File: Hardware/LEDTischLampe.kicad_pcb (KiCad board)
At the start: 2 copper layers, 160 x 160 mm, 135 parts, among them J1 Conn_01x02_Socket, J2 USB_C_Receptacle_USB2.0_14P, J3 Conn_02x03_Counter_Clockwise, Q1 P-CHANNEL-MOSFET, SW1 Reset, SW2 User, U1 ESP32-C3-WROOM-02, U2 SY7200AABC, U3 SY7200AABC, U4 SY7200AABC, U5 SY7200AABC, U6 SY7200AABC, U7 RY8310

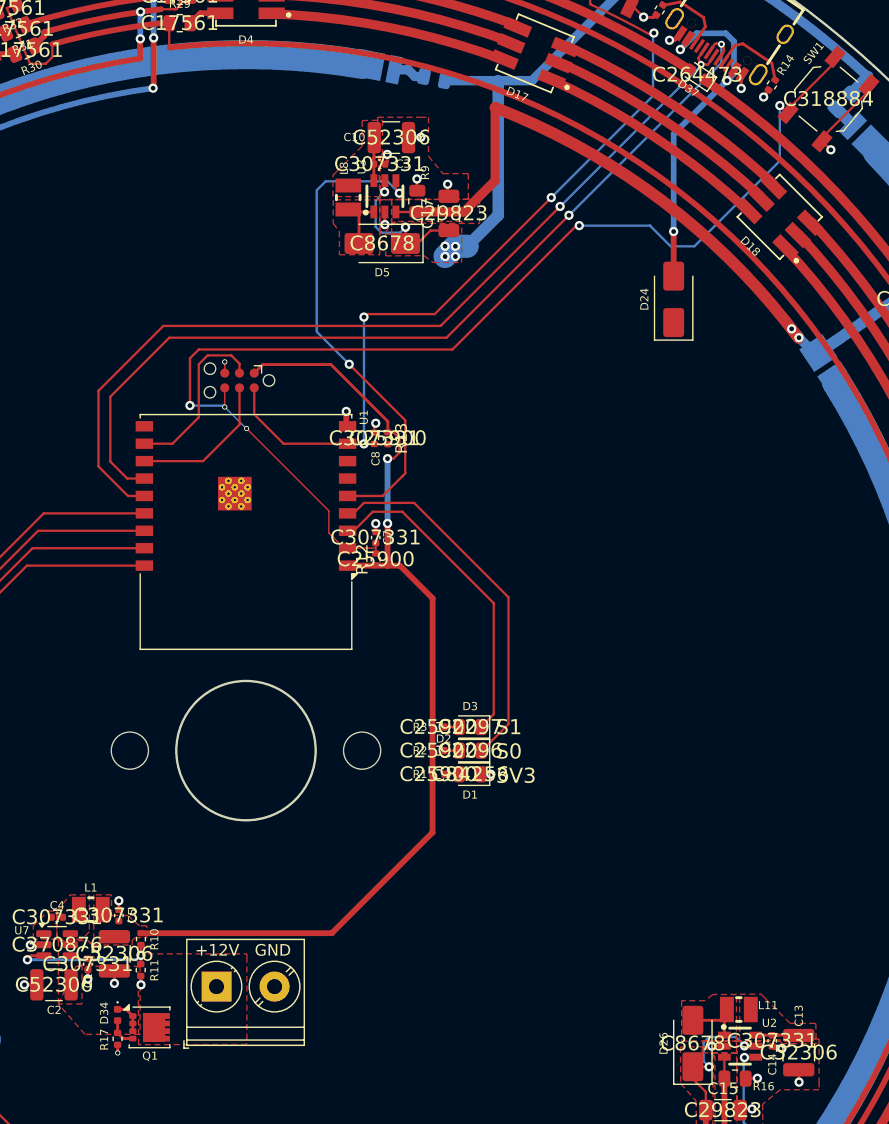
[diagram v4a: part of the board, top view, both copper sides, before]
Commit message: assign remaining LCSC numbers and change R_sense of LED drivers
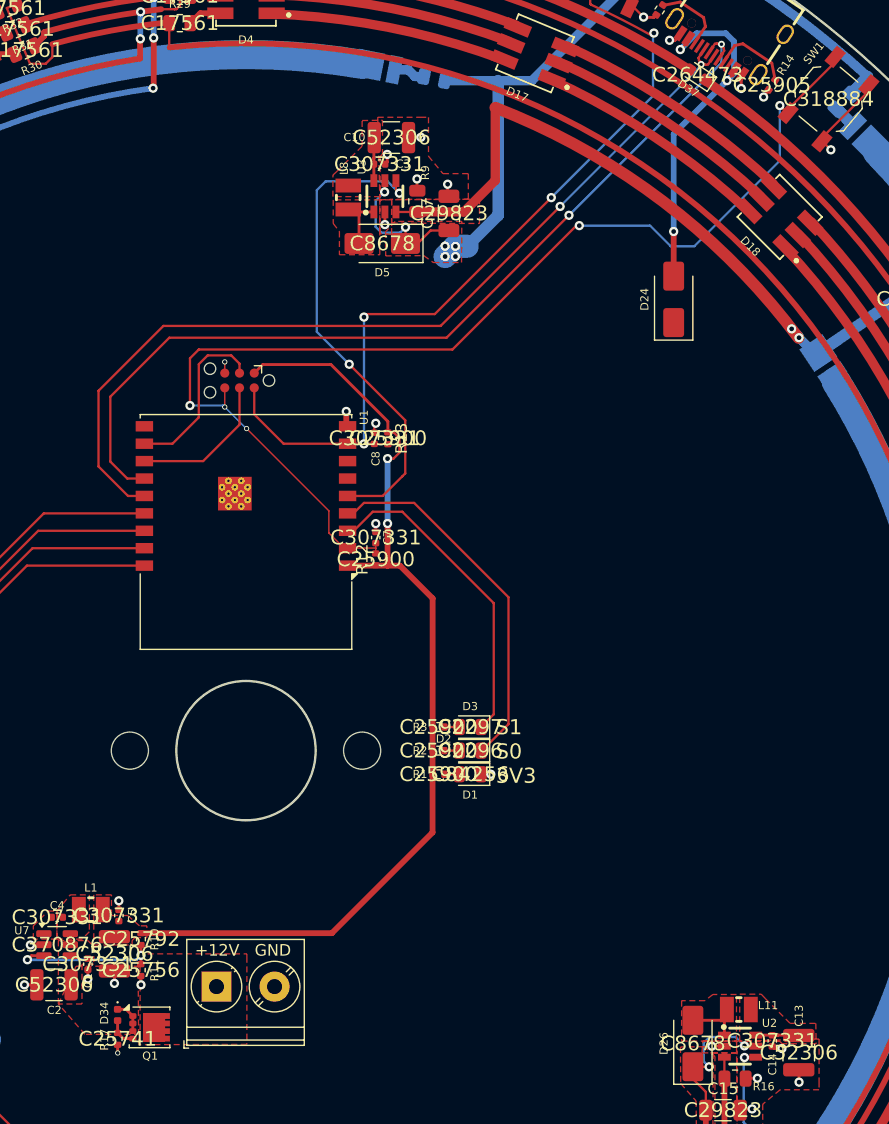
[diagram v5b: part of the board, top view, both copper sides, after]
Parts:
- R16, R26, R27, R8: value 2 -> 3.3
- R9: value 2 -> 0.5
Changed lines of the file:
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@@
 		(sheetname "Root")
 		(sheetfile "LEDTischLampe.kicad_sch")
-		(attr exclude_from_pos_files)
+		(attr exclude_from_pos_files exclude_from_bom)
 		(fp_line
 			(start -1.27 1.27)
@@
 			)
 		)
-		(property "Value" "2"
+		(property "Value" "3.3"
 			(at 0 1.65 0)
 			(layer "F.Fab")
@@
 			)
 		)
-		(property "Description" "Resistor"
+		(property "Description" "Resistor, small symbol"
 			(at 0 0 0)
 			(unlocked yes)
@@
 		)
 		(property ki_fp_filters "R_*")
-		(sheetname "LedTreiber2")
-		(sheetfile "CCLedTreiber.kicad_sch")
+		(sheetname "LedsOben")
+		(sheetfile "LedsOben.kicad_sch")
 		(attr smd)
 		(fp_line
@@
 			)
 		)
+		(property "LCSC" "C25792"
+			(at 0 0 0)
+			(layer "F.SilkS")
+			(effects
+				(font
+					(size 1.27 1.27)
+					(thickness 0.15)
+				)
+			)
+		)
 		(property ki_fp_filters "R_*")
 		(sheetname "Root")
@@
 			)
 		)
+		(property "LCSC" "C25756"
+			(at 0 0 0)
+			(layer "F.SilkS")
+			(effects
+				(font
+					(size 1.27 1.27)
+					(thickness 0.15)
+				)
+			)
+		)
 		(property ki_fp_filters "R_*")
 		(sheetname "Root")
@@
 			)
 		)
-		(property "Value" "2"
+		(property "Value" "0.5"
 			(at 0 1.65 90)
 			(layer "F.Fab")
@@
 			)
 		)
-		(property "Description" "Resistor"
+		(property "Description" "Resistor, small symbol"
 			(at 0 0 90)
 			(unlocked yes)
@@
 		)
 		(property ki_fp_filters "R_*")
-		(sheetname "LedTreiber4")
-		(sheetfile "CCLedTreiber.kicad_sch")
+		(sheetname "LedsUnten")
+		(sheetfile "LedsUnten.kicad_sch")
 		(attr smd)
 		(fp_line
@@
 			)
 		)
+		(property "LCSC" "C25741"
+			(at 0 0 0)
+			(layer "F.SilkS")
+			(effects
+				(font
+					(size 1.27 1.27)
+					(thickness 0.15)
+				)
+			)
+		)
 		(property ki_fp_filters "R_*")
 		(sheetname "Root")
@@
 			)
 		)
+		(property "LCSC" "C25905"
+			(at 0 0 0)
+			(layer "F.SilkS")
+			(effects
+				(font
+					(size 1.27 1.27)
+					(thickness 0.15)
+				)
+			)
+		)
 		(property ki_fp_filters "R_*")
 		(sheetname "Root")
@@
 			)
 		)
-		(property "Value" "2"
+		(property "Value" "3.3"
 			(at 0 1.65 0)
 			(layer "F.Fab")
@@
 			)
 		)
-		(property "Description" "Resistor"
+		(property "Description" "Resistor, small symbol"
 			(at 0 0 0)
 			(unlocked yes)
@@
 		)
 		(property ki_fp_filters "R_*")
-		(sheetname "LedTreiber5")
-		(sheetfile "CCLedTreiber.kicad_sch")
+		(sheetname "LedsOben")
+		(sheetfile "LedsOben.kicad_sch")
 		(attr smd)
 		(fp_line
@@
 			)
 		)
-		(property "Value" "2"
+		(property "Value" "3.3"
 			(at 0 1.65 0)
 			(layer "F.Fab")
@@
 			)
 		)
-		(property "Description" "Resistor"
+		(property "Description" "Resistor, small symbol"
 			(at 0 0 0)
 			(unlocked yes)
@@
 		)
 		(property ki_fp_filters "R_*")
-		(sheetname "LedTreiber3")
-		(sheetfile "CCLedTreiber.kicad_sch")
+		(sheetname "LedsOben")
+		(sheetfile "LedsOben.kicad_sch")
 		(attr smd)
 		(fp_line
@@
 			)
 		)
-		(property "Value" "2"
+		(property "Value" "3.3"
 			(at 0 1.65 0)
 			(layer "F.Fab")
@@
 			)
 		)
-		(property "Description" "Resistor"
+		(property "Description" "Resistor, small symbol"
 			(at 0 0 0)
 			(unlocked yes)
@@
 		)
 		(property ki_fp_filters "R_*")
-		(sheetname "LedTreiber1")
-		(sheetfile "CCLedTreiber.kicad_sch")
+		(sheetname "LedsOben")
+		(sheetfile "LedsOben.kicad_sch")
 		(attr smd)
 		(fp_line

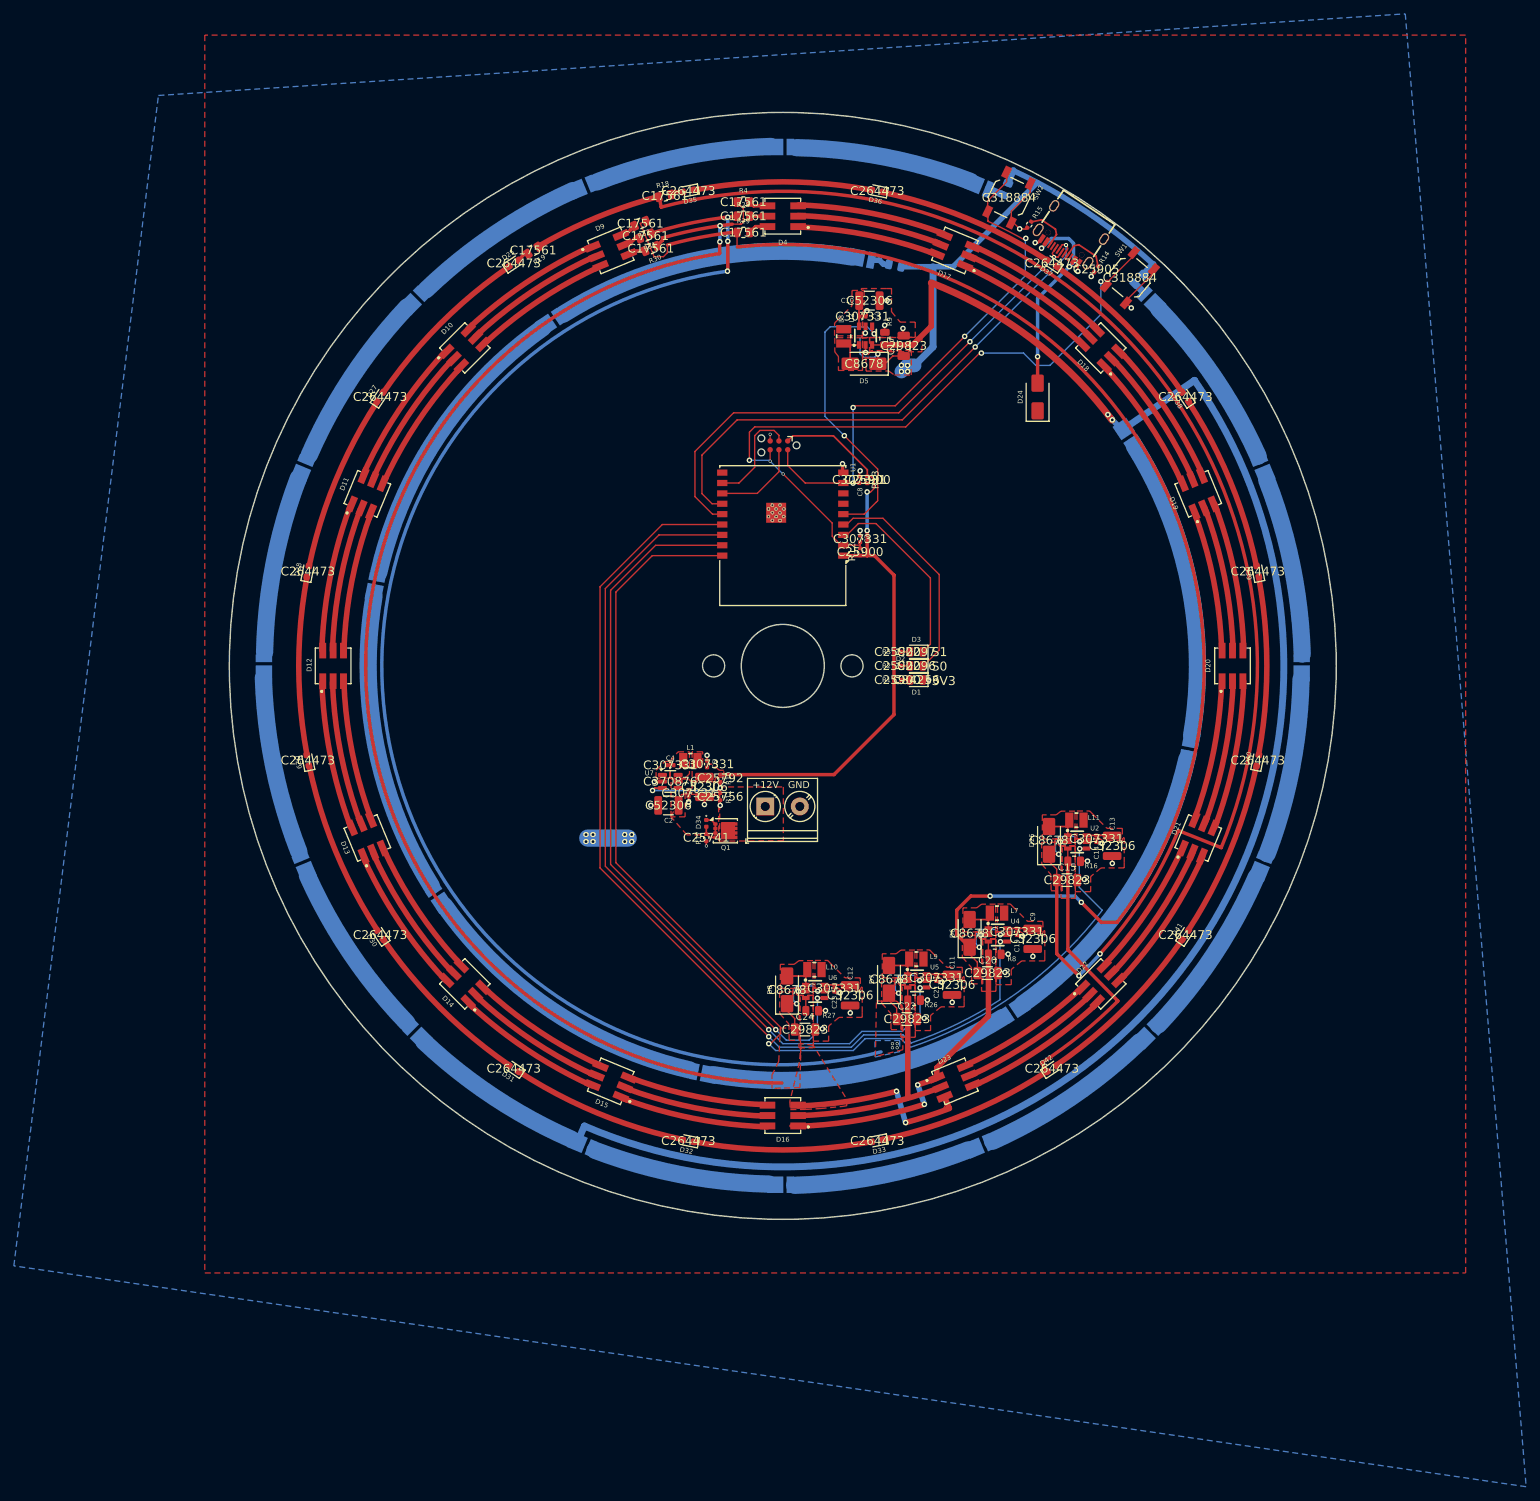
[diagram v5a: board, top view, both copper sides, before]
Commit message: remove LCSC numbers from silkscreen (bug in jlcpcb-tools)
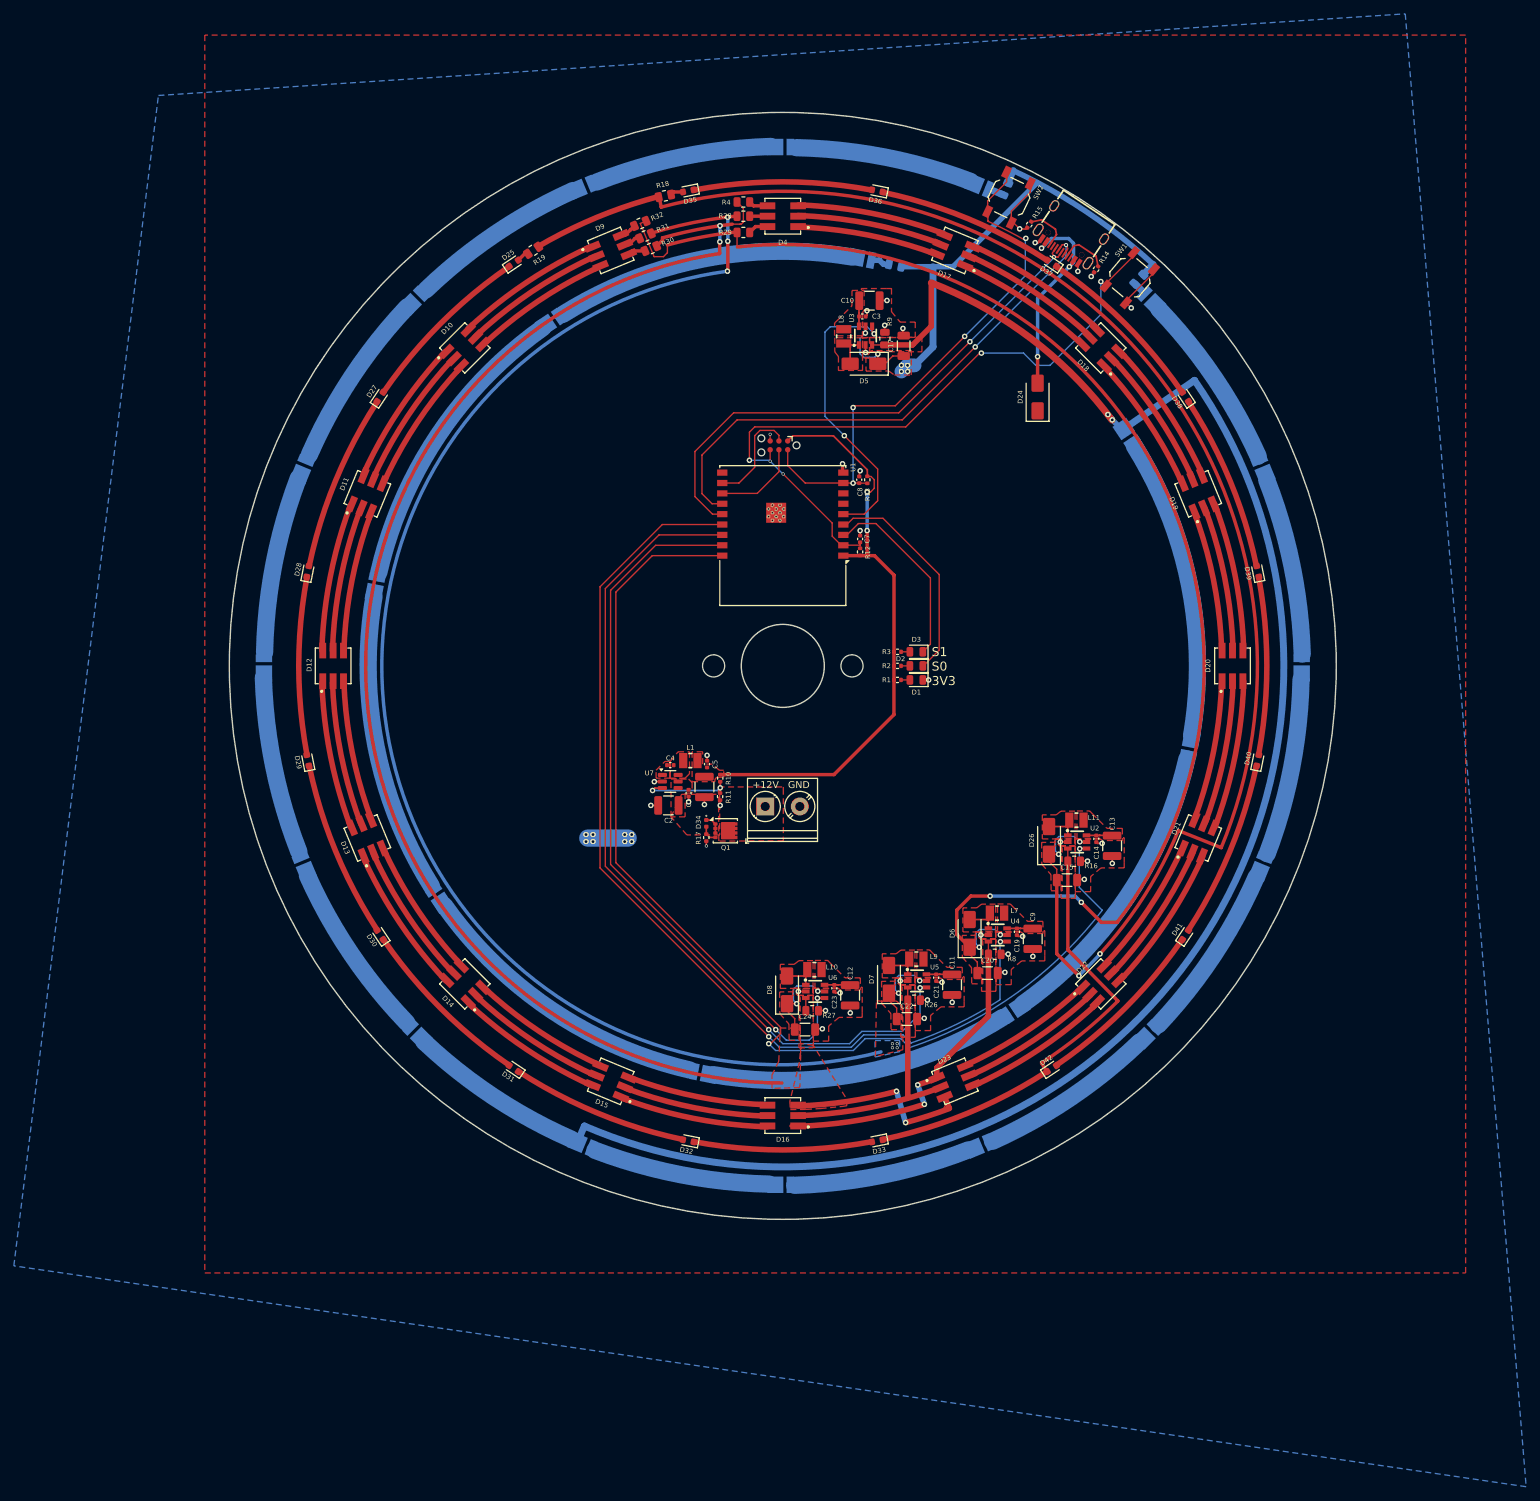
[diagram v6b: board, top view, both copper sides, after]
